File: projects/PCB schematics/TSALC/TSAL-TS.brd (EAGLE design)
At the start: 99.1 x 99.1 mm, 29 parts, among them J1 2P_1-770166-0, J2 2P_1-770166-0, J3 2P_1-770166-0, J4 2P_1-770166-0, X1 5566-2, X2 5566-2

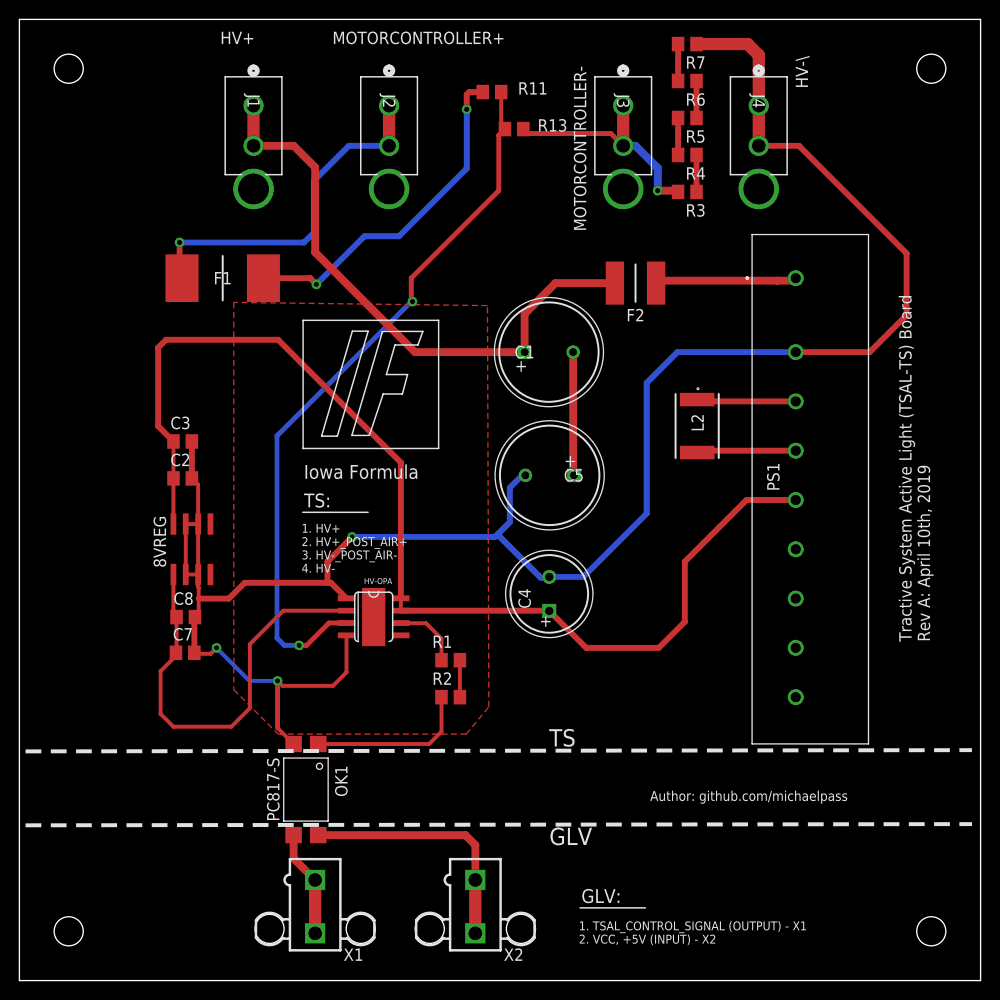
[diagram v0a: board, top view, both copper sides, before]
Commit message: PROJ - Silkscreen modifications - 50%.
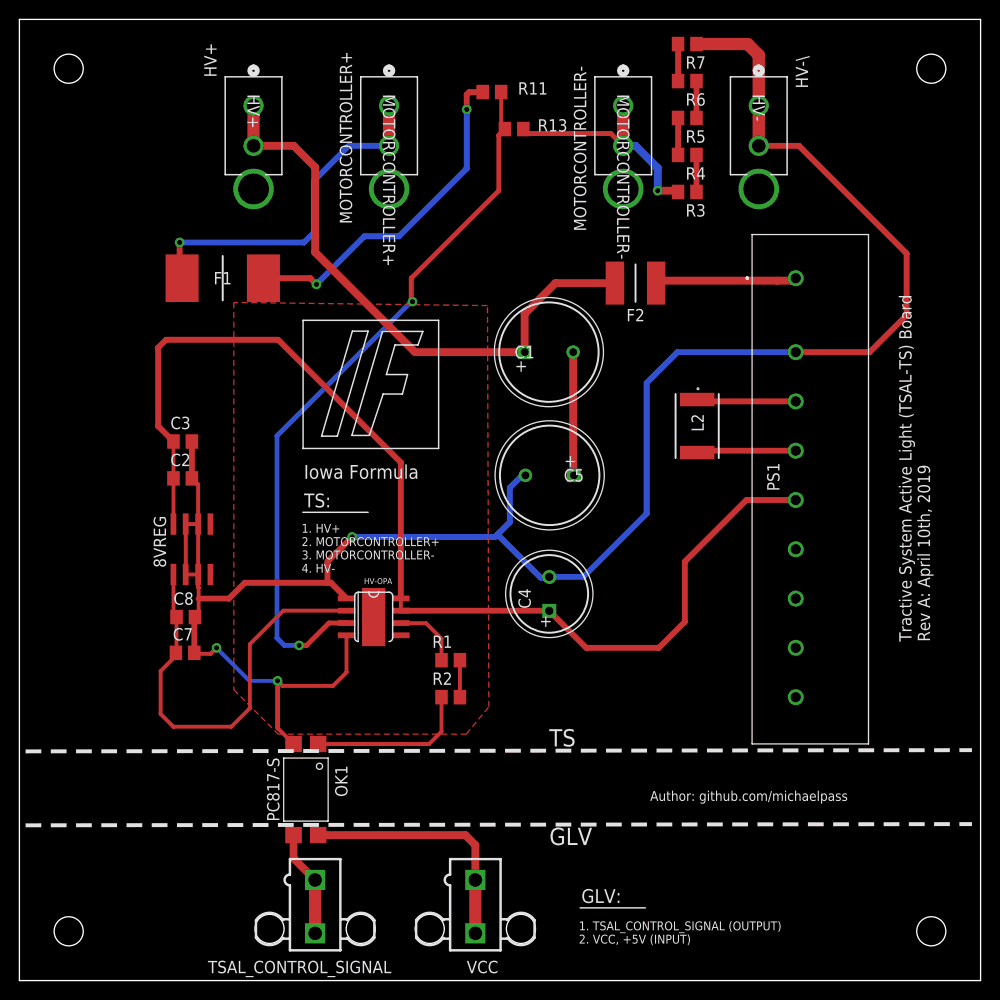
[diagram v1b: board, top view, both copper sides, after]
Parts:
- renumbered J1 to HV+, J2 to MOTORCONTROLLER+, J3 to MOTORCONTROLLER-, J4 to HV-, X1 to TSAL_CONTROL_SIGNAL, X2 to VCC
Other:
- board text added: "1. HV+ 2. MOTORCONTROLLER+ 3. MOTORCONTROLLER- 4. HV-"
- board text added: "1. TSAL_CONTROL_SIGNAL (OUTPUT) 2. VCC, +5V (INPUT)"
- board text removed: "1. HV+ 2. HV+_POST_AIR+ 3. HV-_POST_AIR- 4. HV-"
- board text removed: "1. TSAL_CONTROL_SIGNAL (OUTPUT) - X1 2. VCC, +5V (INPUT) - X2"
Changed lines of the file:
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@@
 <text x="54.61" y="24.13" size="1.778" layer="25">TS</text>
 <text x="54.61" y="13.97" size="1.778" layer="25">GLV</text>
-<text x="20.701" y="96.52" size="1.27" layer="25">HV+</text>
+<text x="20.32" y="93.091" size="1.27" layer="25" rot="R90">HV+</text>
 <text x="81.28" y="91.948" size="1.27" layer="25" rot="R90">HV-\</text>
-<text x="32.258" y="96.52" size="1.27" layer="25">MOTORCONTROLLER+</text>
+<text x="34.29" y="77.978" size="1.27" layer="25" rot="R90">MOTORCONTROLLER+</text>
 <text x="58.42" y="77.216" size="1.27" layer="25" rot="R90">MOTORCONTROLLER-</text>
 <text x="56.134" y="52.959" size="1.27" layer="25">+</text>
@@
 <text x="64.9986" y="18.5166" size="1.016" layer="25" font="vector">Author: github.com/michaelpass</text>
 <text x="57.912" y="8.001" size="1.4224" layer="25" font="vector">GLV:</text>
-<text x="57.658" y="3.81" size="0.9144" layer="25" font="vector">1. TSAL_CONTROL_SIGNAL (OUTPUT) - X1
-2. VCC, +5V (INPUT) - X2</text>
+<text x="57.658" y="3.81" size="0.9144" layer="25" font="vector">1. TSAL_CONTROL_SIGNAL (OUTPUT)
+2. VCC, +5V (INPUT)</text>
 <wire x1="57.785" y1="7.493" x2="64.516" y2="7.493" width="0.1524" layer="25"/>
 <wire x1="29.2354" y1="68.0466" x2="29.2354" y2="54.8386" width="0.1524" layer="25"/>
@@
 <text x="29.337" y="48.768" size="1.4224" layer="25" font="vector">TS:</text>
 <text x="29.083" y="42.037" size="0.9144" layer="25" font="vector">1. HV+
-2. HV+_POST_AIR+
-3. HV-_POST_AIR-
+2. MOTORCONTROLLER+
+3. MOTORCONTROLLER-
 4. HV-</text>
 <wire x1="29.21" y1="48.26" x2="35.941" y2="48.26" width="0.1524" layer="25"/>
@@
 <attribute name="SPICEPREFIX" value="R" x="44.45" y="29.21" size="1.778" layer="27" display="off"/>
 </element>
-<element name="X2" library="con-molex" library_urn="urn:adsk.eagle:library:165" package="5566-2" package3d_urn="urn:adsk.eagle:package:8078583/1" value="5566-2" x="46.99" y="7.62" smashed="yes" rot="R180">
+<element name="VCC" library="con-molex" library_urn="urn:adsk.eagle:library:165" package="5566-2" package3d_urn="urn:adsk.eagle:package:8078583/1" value="5566-2" x="46.99" y="7.62" smashed="yes" rot="R180">
 <attribute name="MF" value="MOLEX" x="46.99" y="7.62" size="1.778" layer="27" rot="R180" display="off"/>
 <attribute name="MPN" value="" x="46.99" y="7.62" size="1.778" layer="27" rot="R180" display="off"/>
-<attribute name="NAME" x="49.911" y="2.032" size="1.27" layer="25"/>
+<attribute name="NAME" x="46.101" y="0.762" size="1.27" layer="25"/>
 <attribute name="OC_FARNELL" value="1822072" x="46.99" y="7.62" size="1.778" layer="27" rot="R180" display="off"/>
 <attribute name="OC_NEWARK" value="unknown" x="46.99" y="7.62" size="1.778" layer="27" rot="R180" display="off"/>
 <attribute name="VALUE" x="49.53" y="13.97" size="1.27" layer="27" rot="R180"/>
 </element>
-<element name="X1" library="con-molex" library_urn="urn:adsk.eagle:library:165" package="5566-2" package3d_urn="urn:adsk.eagle:package:8078583/1" value="5566-2" x="30.48" y="7.62" smashed="yes" rot="R180">
+<element name="TSAL_CONTROL_SIGNAL" library="con-molex" library_urn="urn:adsk.eagle:library:165" package="5566-2" package3d_urn="urn:adsk.eagle:package:8078583/1" value="5566-2" x="30.48" y="7.62" smashed="yes" rot="R180">
 <attribute name="MF" value="MOLEX" x="30.48" y="7.62" size="1.778" layer="27" rot="R180" display="off"/>
 <attribute name="MPN" value="" x="30.48" y="7.62" size="1.778" layer="27" rot="R180" display="off"/>
-<attribute name="NAME" x="33.401" y="2.032" size="1.27" layer="25"/>
+<attribute name="NAME" x="19.431" y="0.762" size="1.27" layer="25"/>
 <attribute name="OC_FARNELL" value="1822072" x="30.48" y="7.62" size="1.778" layer="27" rot="R180" display="off"/>
 <attribute name="OC_NEWARK" value="unknown" x="30.48" y="7.62" size="1.778" layer="27" rot="R180" display="off"/>
@@
 <attribute name="RS_PRICE-STOCK" value="" x="54.61" y="38.1" size="1.778" layer="27" rot="R90" display="off"/>
 </element>
-<element name="J1" library="con-MATE-N-LOK" package="CON2_1X2_P163_VMNL-1MTG" value="2P_1-770166-0" x="24.13" y="90.17" smashed="yes" rot="R270">
+<element name="HV+" library="con-MATE-N-LOK" package="CON2_1X2_P163_VMNL-1MTG" value="2P_1-770166-0" x="24.13" y="90.17" smashed="yes" rot="R270">
 <attribute name="MANUFACTURER_PART_NUMBER" value="17701660" x="24.13" y="90.17" size="1.778" layer="27" rot="R270" display="off"/>
 <attribute name="NAME" x="23.495" y="91.3638" size="1.27" layer="25" ratio="6" rot="SR270"/>
 <attribute name="VENDOR" value="TE Connectivity" x="24.13" y="90.17" size="1.778" layer="27" rot="R270" display="off"/>
 </element>
-<element name="J2" library="con-MATE-N-LOK" package="CON2_1X2_P163_VMNL-1MTG" value="2P_1-770166-0" x="38.1" y="90.17" smashed="yes" rot="R270">
+<element name="MOTORCONTROLLER+" library="con-MATE-N-LOK" package="CON2_1X2_P163_VMNL-1MTG" value="2P_1-770166-0" x="38.1" y="90.17" smashed="yes" rot="R270">
 <attribute name="MANUFACTURER_PART_NUMBER" value="17701660" x="38.1" y="90.17" size="1.778" layer="27" rot="R270" display="off"/>
 <attribute name="NAME" x="37.465" y="91.3638" size="1.27" layer="25" ratio="6" rot="SR270"/>
 <attribute name="VENDOR" value="TE Connectivity" x="38.1" y="90.17" size="1.778" layer="27" rot="R270" display="off"/>
 </element>
-<element name="J3" library="con-MATE-N-LOK" package="CON2_1X2_P163_VMNL-1MTG" value="2P_1-770166-0" x="62.23" y="90.17" smashed="yes" rot="R270">
+<element name="MOTORCONTROLLER-" library="con-MATE-N-LOK" package="CON2_1X2_P163_VMNL-1MTG" value="2P_1-770166-0" x="62.23" y="90.17" smashed="yes" rot="R270">
 <attribute name="MANUFACTURER_PART_NUMBER" value="17701660" x="62.23" y="90.17" size="1.778" layer="27" rot="R270" display="off"/>
 <attribute name="NAME" x="61.595" y="91.3638" size="1.27" layer="25" ratio="6" rot="SR270"/>
 <attribute name="VENDOR" value="TE Connectivity" x="62.23" y="90.17" size="1.778" layer="27" rot="R270" display="off"/>
 </element>
-<element name="J4" library="con-MATE-N-LOK" package="CON2_1X2_P163_VMNL-1MTG" value="2P_1-770166-0" x="76.2" y="90.17" smashed="yes" rot="R270">
+<element name="HV-" library="con-MATE-N-LOK" package="CON2_1X2_P163_VMNL-1MTG" value="2P_1-770166-0" x="76.2" y="90.17" smashed="yes" rot="R270">
 <attribute name="MANUFACTURER_PART_NUMBER" value="17701660" x="76.2" y="90.17" size="1.778" layer="27" rot="R270" display="off"/>
 <attribute name="NAME" x="75.565" y="91.3638" size="1.27" layer="25" ratio="6" rot="SR270"/>
@@
 <contactref element="PS1" pad="4"/>
 <contactref element="C4" pad="2"/>
-<contactref element="J4" pad="1"/>
-<contactref element="J4" pad="2"/>
+<contactref element="HV-" pad="1"/>
+<contactref element="HV-" pad="2"/>
 <contactref element="R7" pad="2"/>
 <wire x1="76.2" y1="90.17" x2="76.2" y2="86.0298" width="1.27" layer="1"/>
@@
 <signal name="VCC">
 <contactref element="OK1" pad="4"/>
-<contactref element="X2" pad="1"/>
-<contactref element="X2" pad="2"/>
+<contactref element="VCC" pad="1"/>
+<contactref element="VCC" pad="2"/>
 <wire x1="46.99" y1="4.87" x2="46.99" y2="10.37" width="1.27" layer="1"/>
 <wire x1="45.9675" y1="14.9925" x2="30.7975" y2="14.9925" width="0.8128" layer="1"/>
@@
 </signal>
 <signal name="TSAL_CONTROL_SIGNAL">
-<contactref element="X1" pad="1"/>
-<contactref element="X1" pad="2"/>
+<contactref element="TSAL_CONTROL_SIGNAL" pad="1"/>
+<contactref element="TSAL_CONTROL_SIGNAL" pad="2"/>
 <contactref element="OK1" pad="3"/>
 <wire x1="30.48" y1="4.87" x2="30.48" y2="10.37" width="1.27" layer="1"/>
@@
 </signal>
 <signal name="HV+">
-<contactref element="J1" pad="1"/>
-<contactref element="J1" pad="2"/>
+<contactref element="HV+" pad="1"/>
+<contactref element="HV+" pad="2"/>
 <wire x1="24.13" y1="90.17" x2="24.13" y2="86.0298" width="1.27" layer="1"/>
 <wire x1="24.13" y1="86.0298" x2="28.2702" y2="86.0298" width="0.8128" layer="1"/>
@@
 </signal>
 <signal name="MOTORCONTROLLER+">
-<contactref element="J2" pad="1"/>
-<contactref element="J2" pad="2"/>
+<contactref element="MOTORCONTROLLER+" pad="1"/>
+<contactref element="MOTORCONTROLLER+" pad="2"/>
 <wire x1="38.1" y1="90.17" x2="38.1" y2="86.0298" width="1.27" layer="1"/>
 <contactref element="F1" pad="1"/>
@@
 </signal>
 <signal name="MOTORCONTROLLER-">
-<contactref element="J3" pad="1"/>
-<contactref element="J3" pad="2"/>
+<contactref element="MOTORCONTROLLER-" pad="1"/>
+<contactref element="MOTORCONTROLLER-" pad="2"/>
 <contactref element="R13" pad="1"/>
 <contactref element="R3" pad="1"/>

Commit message: PROJ - Rgoedken split TSAL signal resistors into smaller resistors for voltage divider; current voltage divider split would have dropped too high a voltage against previous resistor's rated voltage.
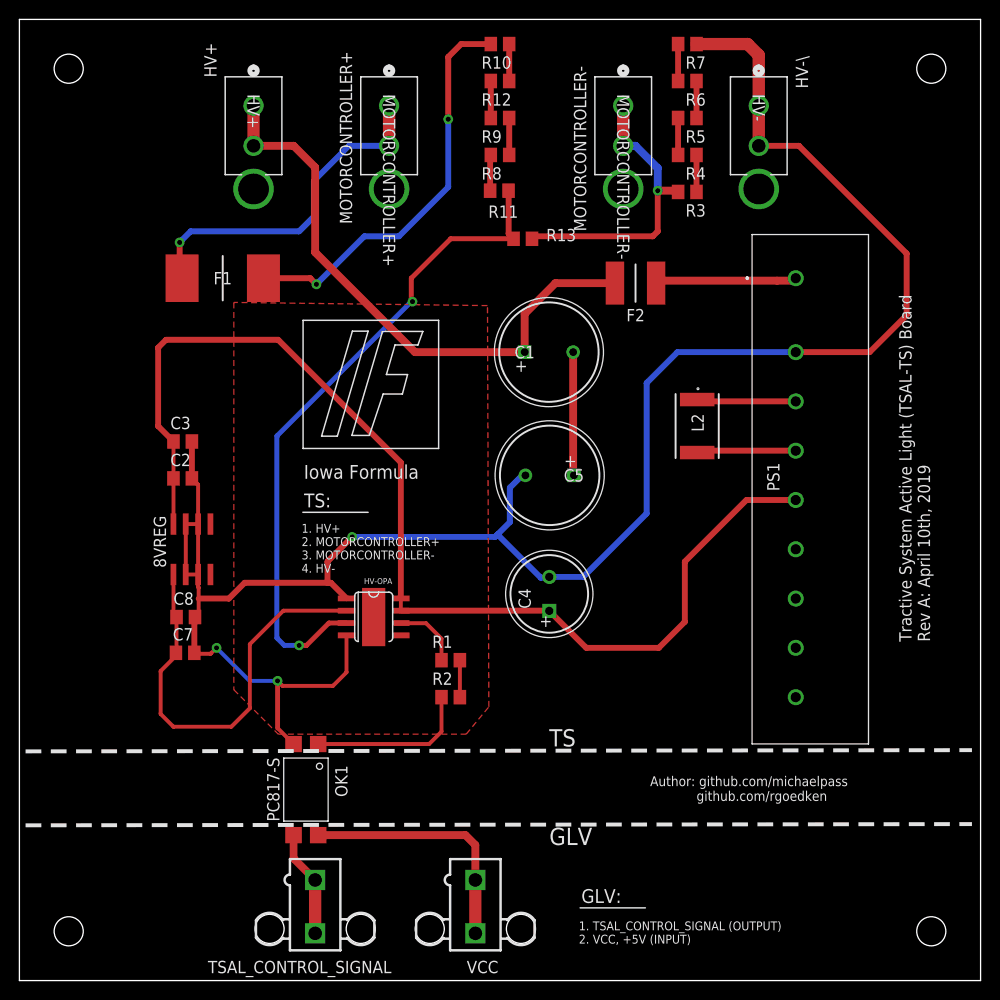
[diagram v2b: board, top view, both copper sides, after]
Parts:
- added R10, R12, R9: 180k, rcl:R0805
- added R8: 100k, rcl:R0805
- R11: value 680k -> 39k
- moved R13 11.3 mm to (51.9, 76.5)
- moved R11 10.2 mm to (49.5, 81.4)
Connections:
- new net N$11: R10.2, R12.1
- new net N$12: R10.1, R9.2
- new net N$13: R8.2, R9.1
- new net N$14: R11.2, R8.1
- net MOTORCONTROLLER+_POST_FUSE: now also R12.2; no longer R11.2
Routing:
- net MOTORCONTROLLER-: track 24.2 -> 30.7 mm
- net MOTORCONTROLLER+_POST_FUSE: track 35.5 -> 41.8 mm
- net SIGNAL_VDIV: track 75.0 -> 71.0 mm
- net N$13: track 0.00 -> 3.81 mm
- net N$11: track 0.00 -> 3.81 mm
- net N$12: track 0.00 -> 3.81 mm
- net N$14: track 0.00 -> 3.71 mm
- net MOTORCONTROLLER+: track 36.8 -> 35.8 mm
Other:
- board text added: "Author: github.com/michaelpass github.com/rgoedken"
- board text removed: "Author: github.com/michaelpass"

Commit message: PROJ - Gerber files major milestone - 05/05/19.
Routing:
- net SIGNAL_VDIV: track 71.0 -> 69.1 mm
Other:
- board text added: "Tractive System Active Light (TSAL-TS) Board Rev A: May 5th, 2019"
- board text removed: "Tractive System Active Light (TSAL-TS) Board Rev A: April 10th, 2019"
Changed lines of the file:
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@@
 <wire x1="0" y1="99.06" x2="0" y2="0" width="0" layer="20"/>
 <text x="93.853" y="34.925" size="1.27" layer="25" font="vector" rot="R90">Tractive System Active Light (TSAL-TS) Board
-Rev A: April 10th, 2019</text>
+Rev A: May 5th, 2019</text>
 <hole x="5.08" y="5.08" drill="3"/>
 <hole x="93.98" y="5.08" drill="3"/>
@@
 <contactref element="R13" pad="2"/>
 <contactref element="R11" pad="1"/>
-<wire x1="50.9295" y1="76.454" x2="49.0245" y2="76.454" width="0.4064" layer="1"/>
 <wire x1="50.9295" y1="76.454" x2="44.45" y2="76.454" width="0.508" layer="1"/>
 <wire x1="44.45" y1="76.454" x2="40.3891875" y2="72.3931875" width="0.508" layer="1"/>
